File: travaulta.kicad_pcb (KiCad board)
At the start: 2 copper layers, 209.7 x 76.4 mm, 2 parts

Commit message: schematics
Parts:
- removed REF**: LED_0201_0603Metric_Pad0.64x0.40mm_HandSolder, LED_SMD:LED_0201_0603Metric_Pad0.64x0.40mm_HandSolder
- removed REF**: LED_0603_1608Metric_Pad1.05x0.95mm_HandSolder, LED_SMD:LED_0603_1608Metric_Pad1.05x0.95mm_HandSolder
- added C_USBSHIELD1: 4.7nF, Capacitor_SMD:C_0402_1005Metric, B.Cu at (107.3, 23.8)
- added D1: PRTR5V0U2X, Package_TO_SOT_SMD:SOT-143, B.Cu at (113.9, 29.9)
- added F_USBC1: 500mA, Fuse:Fuse_1206_3216Metric, B.Cu at (129.8, 30.5)
- added J1: USB_C_Receptacle_USB2.0, Connector_USB:USB_C_Receptacle_HRO_TYPE-C-31-M-12, B.Cu at (82.5, 49.7)
- added Q1: 2N7002, Package_TO_SOT_SMD:SOT-23, B.Cu at (124.6, 31.1)
- added R1: 100, Resistor_SMD:R_0402_1005Metric, B.Cu at (105.3, 19.4)
- added R2: 100, Resistor_SMD:R_0402_1005Metric, B.Cu at (117.8, 33.1)
- added R4: 100k, Resistor_SMD:R_0402_1005Metric, B.Cu at (120.7, 32.6)
- added R7: 10k, Resistor_SMD:R_0402_1005Metric, B.Cu at (110.2, 23.8)
- added R_USB1: 5.1k, Resistor_SMD:R_0402_1005Metric, B.Cu at (131.2, 33.1)
- added R_USB2: 5.1k, Resistor_SMD:R_0402_1005Metric, B.Cu at (128.3, 34.3)
- added R_USBSHIELD1: 1M, Resistor_SMD:R_0402_1005Metric, B.Cu at (125.4, 34.3)
- added SW1: EC_SW, cipulot_parts:ecs_pad_1U_no_ring, F.Cu at (54.0, 57.1)
- added SW10: EC_SW, cipulot_parts:ecs_pad_1U_no_ring, F.Cu at (225.4, 57.1)
- added SW11: EC_SW, cipulot_parts:ecs_pad_1U_no_ring, F.Cu at (244.5, 57.1)
- added SW12: EC_SW, cipulot_parts:ecs_pad_1U_no_ring, F.Cu at (56.4, 76.2)
- added SW13: EC_SW, cipulot_parts:ecs_pad_1U_no_ring, F.Cu at (77.8, 76.2)
- added SW14: EC_SW, cipulot_parts:ecs_pad_1U_no_ring, F.Cu at (96.8, 76.2)
- added SW15: EC_SW, cipulot_parts:ecs_pad_1U_no_ring, F.Cu at (115.9, 76.2)
- added SW16: EC_SW, cipulot_parts:ecs_pad_1U_no_ring, F.Cu at (134.9, 76.2)
- added SW17: EC_SW, cipulot_parts:ecs_pad_1U_no_ring, F.Cu at (154.0, 76.2)
- added SW18: EC_SW, cipulot_parts:ecs_pad_1U_no_ring, F.Cu at (173.0, 76.2)
- added SW19: EC_SW, cipulot_parts:ecs_pad_1U_no_ring, F.Cu at (192.1, 76.2)
- added SW2: EC_SW, cipulot_parts:ecs_pad_1U_no_ring, F.Cu at (73.0, 57.1)
- added SW20: EC_SW, cipulot_parts:ecs_pad_1U_no_ring, F.Cu at (211.1, 76.2)
- added SW21: EC_SW, cipulot_parts:ecs_pad_1U_no_ring, F.Cu at (237.3, 76.2)
- added SW22: EC_SW, cipulot_parts:ecs_pad_1U_no_ring, F.Cu at (61.1, 95.2)
- added SW23: EC_SW, cipulot_parts:ecs_pad_1U_no_ring, F.Cu at (87.3, 95.2)
- added SW24: EC_SW, cipulot_parts:ecs_pad_1U_no_ring, F.Cu at (106.4, 95.2)
- added SW25: EC_SW, cipulot_parts:ecs_pad_1U_no_ring, F.Cu at (125.4, 95.2)
- added SW26: EC_SW, cipulot_parts:ecs_pad_1U_no_ring, F.Cu at (144.5, 95.2)
- added SW27: EC_SW, cipulot_parts:ecs_pad_1U_no_ring, F.Cu at (163.5, 95.2)
- added SW28: EC_SW, cipulot_parts:ecs_pad_1U_no_ring, F.Cu at (182.6, 95.2)
- added SW29: EC_SW, cipulot_parts:ecs_pad_1U_no_ring, F.Cu at (201.6, 95.2)
- added SW3: EC_SW, cipulot_parts:ecs_pad_1U_no_ring, F.Cu at (92.1, 57.1)
- added SW30: EC_SW, cipulot_parts:ecs_pad_1U_no_ring, F.Cu at (220.7, 95.2)
- added SW31: EC_SW, cipulot_parts:ecs_pad_1U_no_ring, F.Cu at (242.1, 95.2)
- added SW32: EC_SW, cipulot_parts:ecs_pad_1U_no_ring, F.Cu at (82.5, 114.3)
- added SW33: EC_SW, cipulot_parts:ecs_pad_1U_no_ring, F.Cu at (104.0, 114.3)
- added SW34: EC_SW, cipulot_parts:ecs_pad_1U_no_ring, F.Cu at (132.6, 114.3)
- added SW35: EC_SW, cipulot_parts:ecs_pad_1U_no_ring, F.Cu at (165.9, 114.3)
- added SW36: EC_SW, cipulot_parts:ecs_pad_1U_no_ring, F.Cu at (194.5, 114.3)
- added SW37: EC_SW, cipulot_parts:ecs_pad_1U_no_ring, F.Cu at (215.9, 114.3)
- added SW4: EC_SW, cipulot_parts:ecs_pad_1U_no_ring, F.Cu at (111.1, 57.1)
- added SW5: EC_SW, cipulot_parts:ecs_pad_1U_no_ring, F.Cu at (130.2, 57.1)
- added SW6: EC_SW, cipulot_parts:ecs_pad_1U_no_ring, F.Cu at (149.2, 57.1)
- added SW7: EC_SW, cipulot_parts:ecs_pad_1U_no_ring, F.Cu at (168.3, 57.1)
- added SW8: EC_SW, cipulot_parts:ecs_pad_1U_no_ring, F.Cu at (187.3, 57.1)
- added SW9: EC_SW, cipulot_parts:ecs_pad_1U_no_ring, F.Cu at (206.4, 57.1)
- added U1: STM32F411CCUx, Package_DFN_QFN:QFN-48-1EP_7x7mm_P0.5mm_EP5.6x5.6mm, B.Cu at (116.3, 23.0)
- added U2: XC6206PxxxMR, Package_TO_SOT_SMD:SOT-23, B.Cu at (109.2, 20.6)
- added Y1: 16 MHz, Crystal:Resonator_SMD_Murata_CSTxExxV-3Pin_3.0x1.1mm, B.Cu at (118.4, 29.4)
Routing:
- added copper zone on B.Cu, net GND
- added copper zone on F.Cu, net GND

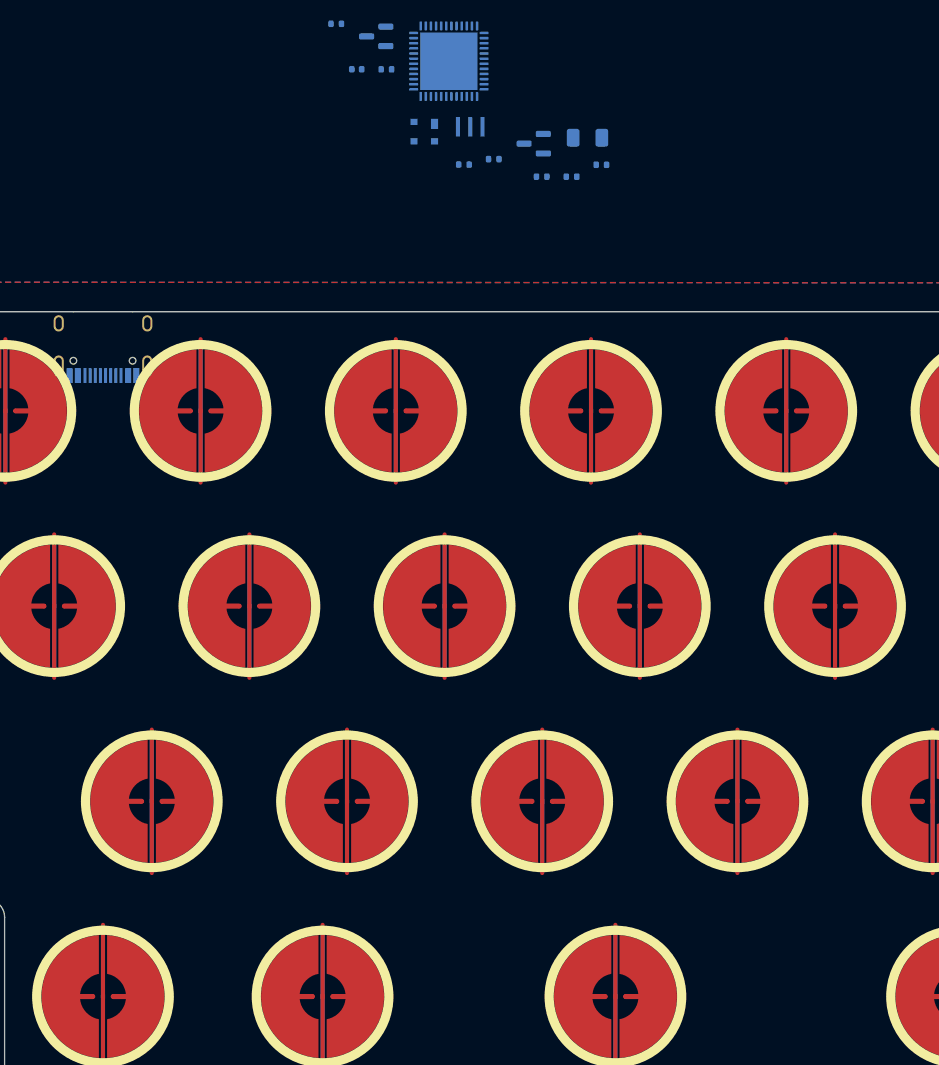
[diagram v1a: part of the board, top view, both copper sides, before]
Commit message: switch footprints plaed
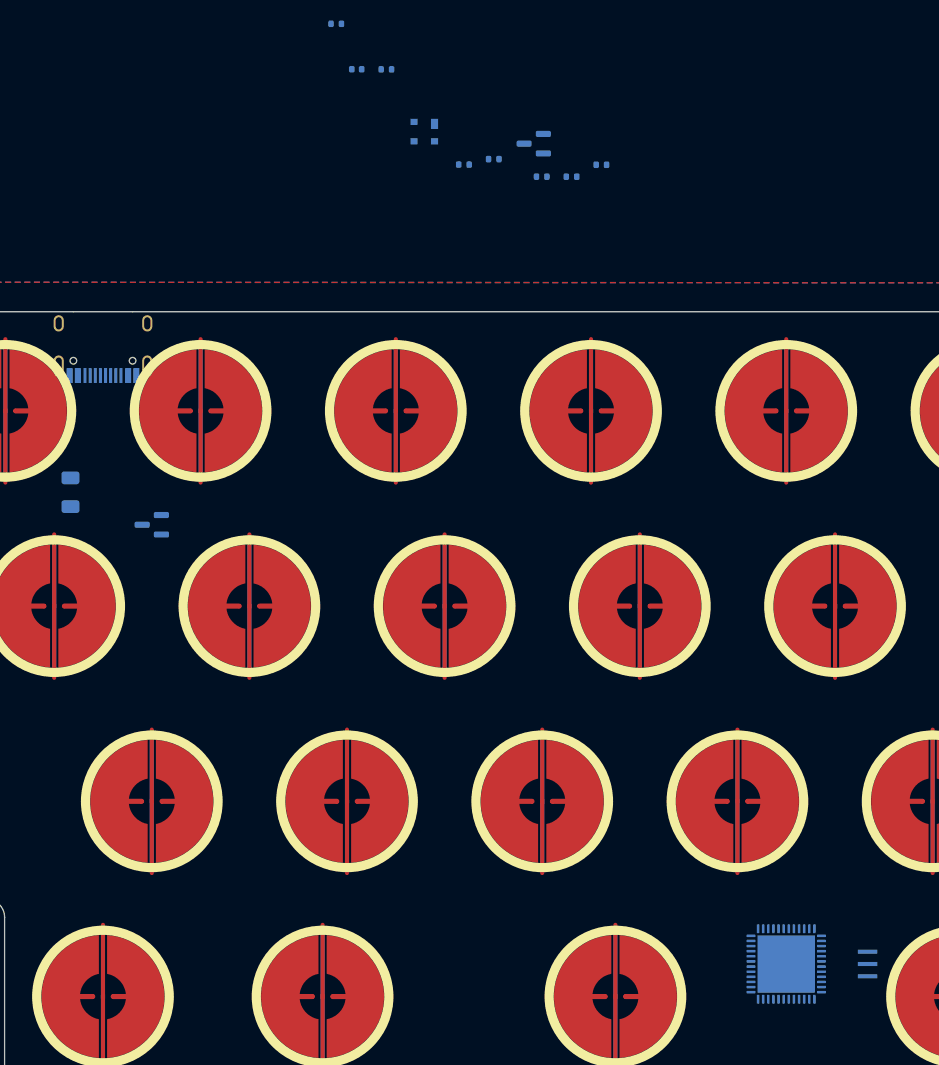
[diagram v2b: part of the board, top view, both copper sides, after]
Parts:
- moved U1 94.1 mm to (149.2, 111.1)
- moved Y1 90.4 mm to (157.2, 111.1), turned to 90 degrees
- moved F_USBC1 61.2 mm to (79.4, 65.1), turned to -90 degrees
- moved U2 52.5 mm to (87.3, 68.3)
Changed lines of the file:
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@@
   )
   (footprint "Crystal:Resonator_SMD_Murata_CSTxExxV-3Pin_3.0x1.1mm" (layer "B.Cu")
-    (at 118.387738 29.4275 180)
+    (at 157.1625 111.125 90)
     (descr "SMD Resomator/Filter Murata CSTCE, https://www.murata.com/en-eu/products/productdata/8801162264606/SPEC-CSTNE16M0VH3C000R0.pdf")
     (tags "SMD SMT ceramic resonator filter")
@@
     (property "Sheetname" "")
     (attr smd)
-    (fp_text reference "Y1" (at 0 2) (layer "B.SilkS")
-      (effects (font (size 1 1) (thickness 0.15)) (justify mirror))
-    )
-    (fp_text value "16 MHz" (at 0 -1.8) (layer "B.Fab")
+    (fp_text reference "Y1" (at 0 2 90) (layer "B.SilkS")
+      (effects (font (size 1 1) (thickness 0.15)) (justify mirror))
+    )
+    (fp_text value "16 MHz" (at 0 -1.8 90) (layer "B.Fab")
       (effects (font (size 0.2 0.2) (thickness 0.03)) (justify mirror))
     )
-    (fp_text user "${REFERENCE}" (at 0.1 0.05) (layer "B.Fab")
+    (fp_text user "${REFERENCE}" (at 0.1 0.05 90) (layer "B.Fab")
       (effects (font (size 0.6 0.6) (thickness 0.08)) (justify mirror))
     )
@@
     (fp_line (start -1.5 -0.3) (end -1.5 0.8) (layer "B.Fab") (width 0.1))
     (fp_line (start 1.5 -0.8) (end 1.5 0.8) (layer "B.Fab") (width 0.1))
-    (pad "1" smd rect (at -1.2 0 180) (size 0.4 1.9) (layers "B.Cu" "B.Paste" "B.Mask")
+    (pad "1" smd rect (at -1.2 0 90) (size 0.4 1.9) (layers "B.Cu" "B.Paste" "B.Mask")
       (net 37 "XTAL1") (pinfunction "1") (pintype "passive"))
-    (pad "2" smd rect (at 0 0 180) (size 0.4 1.9) (layers "B.Cu" "B.Paste" "B.Mask")
+    (pad "2" smd rect (at 0 0 90) (size 0.4 1.9) (layers "B.Cu" "B.Paste" "B.Mask")
       (net 2 "GND") (pinfunction "2") (pintype "passive"))
-    (pad "3" smd rect (at 1.2 0 180) (size 0.4 1.9) (layers "B.Cu" "B.Paste" "B.Mask")
+    (pad "3" smd rect (at 1.2 0 90) (size 0.4 1.9) (layers "B.Cu" "B.Paste" "B.Mask")
       (net 36 "XTAL0") (pinfunction "3") (pintype "passive"))
     (model "${KICAD6_3DMODEL_DIR}/Crystal.3dshapes/Resonator_SMD_Murata_CSTxExxV-3Pin_3.0x1.1mm.wrl"
@@
   )
   (footprint "Package_DFN_QFN:QFN-48-1EP_7x7mm_P0.5mm_EP5.6x5.6mm" (layer "B.Cu")
-    (at 116.302738 23.0225 180)
+    (at 149.225 111.125 180)
     (descr "QFN, 48 Pin (http://www.st.com/resource/en/datasheet/stm32f042k6.pdf#page=94), generated with kicad-footprint-generator ipc_noLead_generator.py")
     (tags "QFN NoLead")
@@
   )
   (footprint "Fuse:Fuse_1206_3216Metric" (layer "B.Cu")
-    (at 129.832738 30.4925 180)
+    (at 79.375 65.0875 -90)
     (descr "Fuse SMD 1206 (3216 Metric), square (rectangular) end terminal, IPC_7351 nominal, (Body size source: http://www.tortai-tech.com/upload/download/2011102023233369053.pdf), generated with kicad-footprint-generator")
     (tags "fuse")
@@
     (property "Sheetname" "")
     (attr smd)
-    (fp_text reference "F_USBC1" (at 0 1.82) (layer "B.SilkS")
-      (effects (font (size 1 1) (thickness 0.15)) (justify mirror))
-    )
-    (fp_text value "500mA" (at 0 -1.82) (layer "B.Fab")
-      (effects (font (size 1 1) (thickness 0.15)) (justify mirror))
-    )
-    (fp_text user "${REFERENCE}" (at 0 0) (layer "B.Fab")
+    (fp_text reference "F_USBC1" (at 0 1.82 90) (layer "B.SilkS")
+      (effects (font (size 1 1) (thickness 0.15)) (justify mirror))
+    )
+    (fp_text value "500mA" (at 0 -1.82 90) (layer "B.Fab")
+      (effects (font (size 1 1) (thickness 0.15)) (justify mirror))
+    )
+    (fp_text user "${REFERENCE}" (at 0 0 90) (layer "B.Fab")
       (effects (font (size 0.8 0.8) (thickness 0.12)) (justify mirror))
     )
@@
     (fp_line (start 1.6 0.8) (end 1.6 -0.8) (layer "B.Fab") (width 0.1))
     (fp_line (start -1.6 -0.8) (end -1.6 0.8) (layer "B.Fab") (width 0.1))
-    (pad "1" smd roundrect (at -1.4 0 180) (size 1.25 1.75) (layers "B.Cu" "B.Paste" "B.Mask") (roundrect_rratio 0.2)
+    (pad "1" smd roundrect (at -1.4 0 270) (size 1.25 1.75) (layers "B.Cu" "B.Paste" "B.Mask") (roundrect_rratio 0.2)
       (net 5 "VCC") (pintype "passive"))
-    (pad "2" smd roundrect (at 1.4 0 180) (size 1.25 1.75) (layers "B.Cu" "B.Paste" "B.Mask") (roundrect_rratio 0.2)
+    (pad "2" smd roundrect (at 1.4 0 270) (size 1.25 1.75) (layers "B.Cu" "B.Paste" "B.Mask") (roundrect_rratio 0.2)
       (net 6 "+5V") (pintype "passive"))
     (model "${KICAD6_3DMODEL_DIR}/Fuse.3dshapes/Fuse_1206_3216Metric.wrl"
@@
   )
   (footprint "Package_TO_SOT_SMD:SOT-23" (layer "B.Cu")
-    (at 109.212738 20.6025 180)
+    (at 87.3125 68.2625 180)
     (descr "SOT, 3 Pin (https://www.jedec.org/system/files/docs/to-236h.pdf variant AB), generated with kicad-footprint-generator ipc_gullwing_generator.py")
     (tags "SOT TO_SOT_SMD")
